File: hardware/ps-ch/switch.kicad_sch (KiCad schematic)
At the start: 18 parts, among them Q4 PSMN059-150Y, Q9 PSMN059-150Y, U16 LM74502H, U18 74LVC126A, U20 74LVC126A

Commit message: improved circuit
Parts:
- U20: footprint (none) -> Package_SO:TSSOP-14_4.4x5mm_P0.65mm; Manufacturer (none) -> Nexperia; Manufacturer Part Number (none) -> 74LVC126APW,118
- U20: renamed from U18; footprint (none) -> Package_SO:TSSOP-14_4.4x5mm_P0.65mm; Manufacturer (none) -> Nexperia; Manufacturer Part Number (none) -> 74LVC126APW,118
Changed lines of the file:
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@@
 			)
 		)
-		(property "Footprint" ""
+		(property "Footprint" "Package_SO:TSSOP-14_4.4x5mm_P0.65mm"
 			(at 147.32 167.64 0)
 			(effects
@@
 			)
 		)
-		(property "Datasheet" ""
+		(property "Datasheet" "https://assets.nexperia.com/documents/data-sheet/74LVC126A.pdf"
 			(at 147.32 167.64 0)
 			(effects
@@
 		)
 		(property "Description" ""
+			(at 147.32 167.64 0)
+			(effects
+				(font
+					(size 1.27 1.27)
+				)
+				(hide yes)
+			)
+		)
+		(property "Manufacturer" "Nexperia"
+			(at 147.32 167.64 0)
+			(effects
+				(font
+					(size 1.27 1.27)
+				)
+				(hide yes)
+			)
+		)
+		(property "Manufacturer Part Number" "74LVC126APW,118"
 			(at 147.32 167.64 0)
 			(effects
@@
 			)
 		)
-		(property "Footprint" ""
+		(property "Footprint" "Package_SO:TSSOP-14_4.4x5mm_P0.65mm"
 			(at 63.5 167.64 0)
 			(effects
@@
 			)
 		)
-		(property "Datasheet" ""
+		(property "Datasheet" "https://assets.nexperia.com/documents/data-sheet/74LVC126A.pdf"
 			(at 63.5 167.64 0)
 			(effects
@@
 		)
 		(property "Description" ""
+			(at 63.5 167.64 0)
+			(effects
+				(font
+					(size 1.27 1.27)
+				)
+				(hide yes)
+			)
+		)
+		(property "Manufacturer" "Nexperia"
+			(at 63.5 167.64 0)
+			(effects
+				(font
+					(size 1.27 1.27)
+				)
+				(hide yes)
+			)
+		)
+		(property "Manufacturer Part Number" "74LVC126APW,118"
 			(at 63.5 167.64 0)
 			(effects
@@
 			)
 		)
-		(property "Footprint" ""
+		(property "Footprint" "Package_SO:TSSOP-14_4.4x5mm_P0.65mm"
 			(at 96.52 167.64 0)
 			(effects
@@
 			)
 		)
-		(property "Datasheet" ""
+		(property "Datasheet" "https://assets.nexperia.com/documents/data-sheet/74LVC126A.pdf"
 			(at 96.52 167.64 0)
 			(effects
@@
 		)
 		(property "Description" ""
+			(at 96.52 167.64 0)
+			(effects
+				(font
+					(size 1.27 1.27)
+				)
+				(hide yes)
+			)
+		)
+		(property "Manufacturer" "Nexperia"
+			(at 96.52 167.64 0)
+			(effects
+				(font
+					(size 1.27 1.27)
+				)
+				(hide yes)
+			)
+		)
+		(property "Manufacturer Part Number" "74LVC126APW,118"
 			(at 96.52 167.64 0)
 			(effects
@@
 		(dnp no)
 		(fields_autoplaced yes)
-		(property "Reference" "U18"
+		(property "Reference" "U20"
 			(at 143.51 107.8798 0)
 			(effects
@@
 			)
 		)
-		(property "Footprint" ""
+		(property "Footprint" "Package_SO:TSSOP-14_4.4x5mm_P0.65mm"
 			(at 132.08 114.3 0)
 			(effects
@@
 			)
 		)
-		(property "Datasheet" ""
+		(property "Datasheet" "https://assets.nexperia.com/documents/data-sheet/74LVC126A.pdf"
 			(at 132.08 114.3 0)
 			(effects
@@
 			)
 		)
+		(property "Manufacturer" "Nexperia"
+			(at 132.08 114.3 0)
+			(effects
+				(font
+					(size 1.27 1.27)
+				)
+				(hide yes)
+			)
+		)
+		(property "Manufacturer Part Number" "74LVC126APW,118"
+			(at 132.08 114.3 0)
+			(effects
+				(font
+					(size 1.27 1.27)
+				)
+				(hide yes)
+			)
+		)
 		(pin "5"
 		)
@@
 			(project "ps-ch"
 				(path "/431acd2e-2ab9-4aa9-b759-273f044decc5/8b075681-8e5e-4240-bfaa-b14997f80de9"
-					(reference "U18")
+					(reference "U20")
 					(unit 1)
 				)

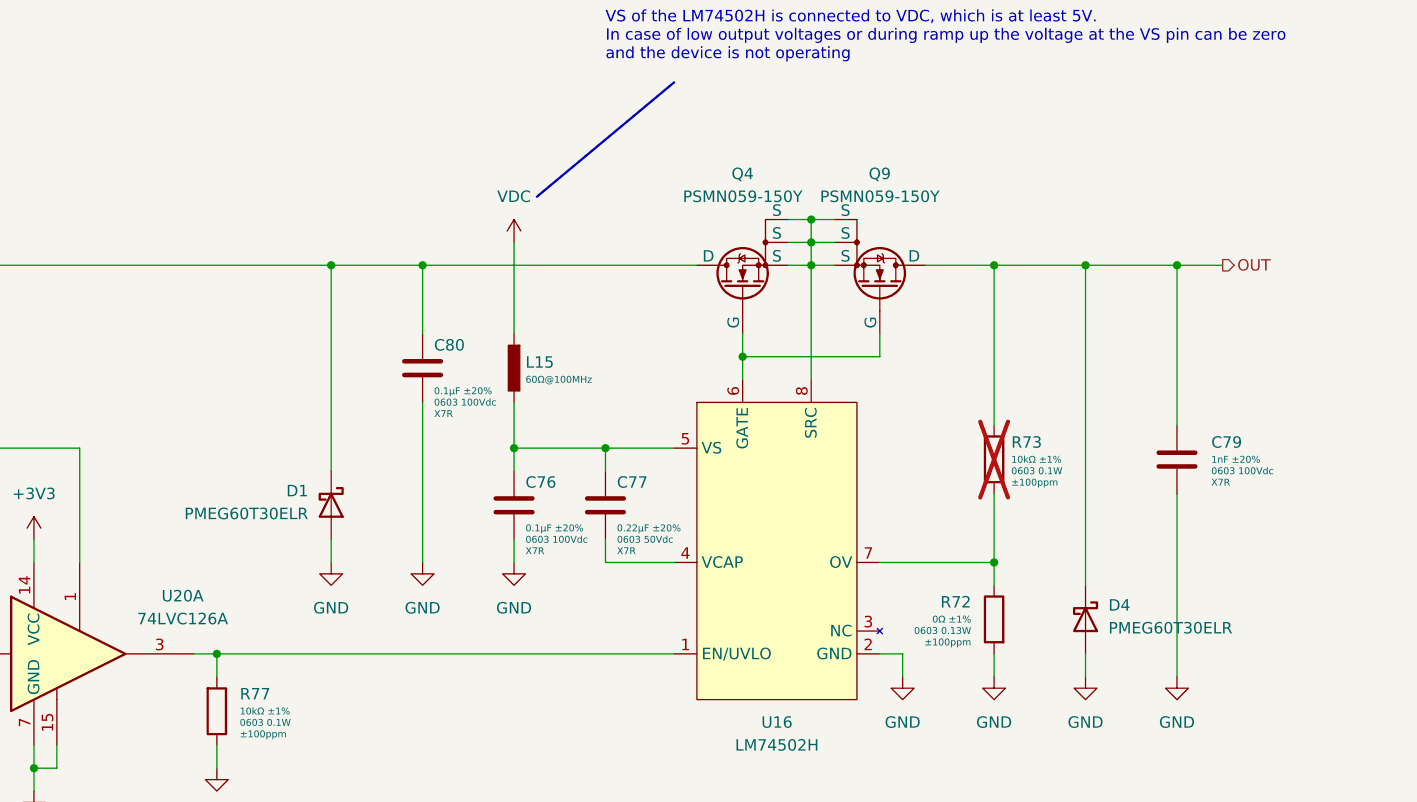
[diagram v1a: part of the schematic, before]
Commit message: added snubber circuit components
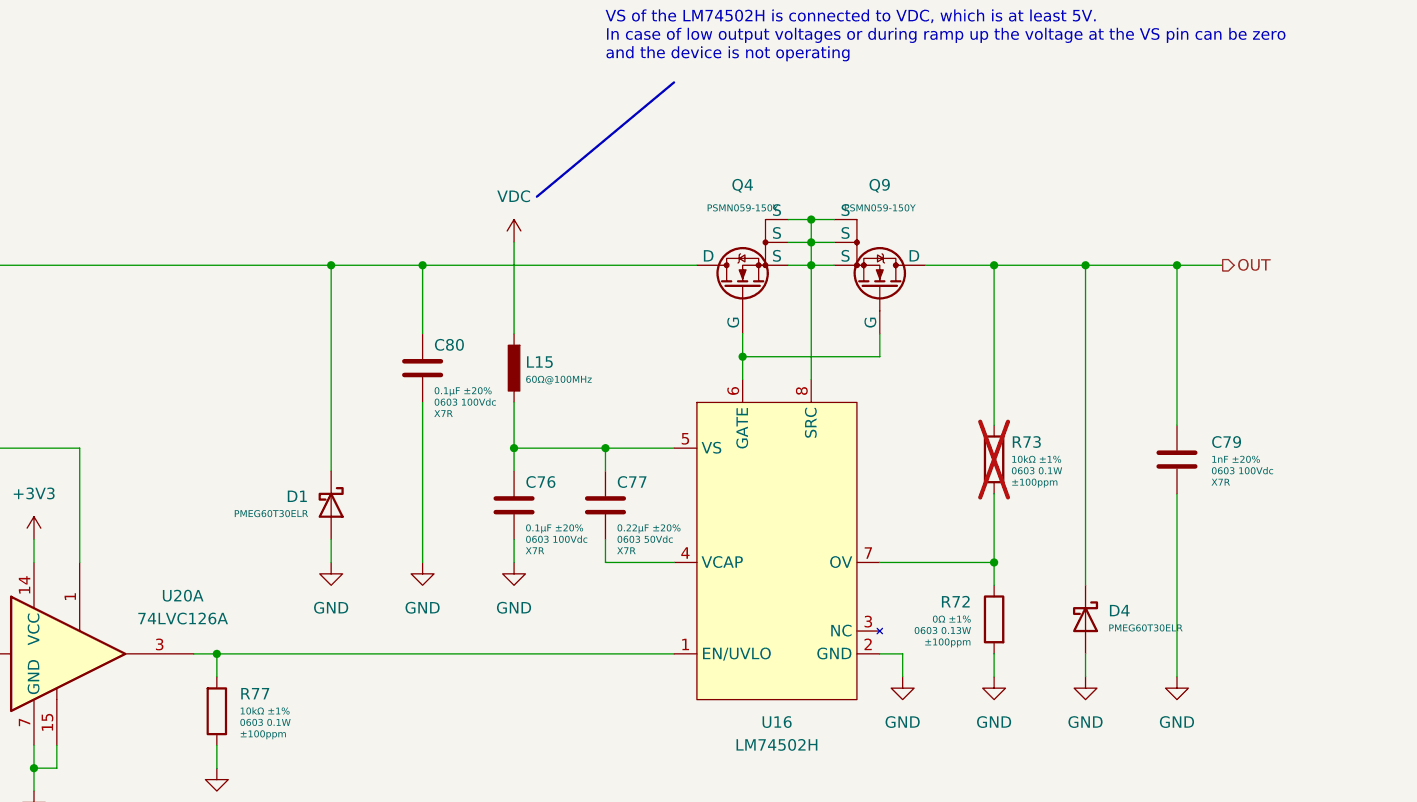
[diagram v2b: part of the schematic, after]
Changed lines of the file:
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@@
 		(on_board yes)
 		(dnp no)
+		(fields_autoplaced yes)
 		(property "Reference" "Q9"
-			(at 220.98 60.96 90)
+			(at 220.98 62.23 90)
 			(effects
 				(font
@@
 		)
 		(property "Value" "PSMN059-150Y"
-			(at 220.98 63.5 90)
-			(effects
-				(font
-					(size 1.27 1.27)
+			(at 220.98 64.77 90)
+			(effects
+				(font
+					(size 0.762 0.762)
+					(color 132 0 132 1)
 				)
 			)
@@
 		(fields_autoplaced yes)
 		(property "Reference" "Q4"
-			(at 205.74 60.96 90)
+			(at 205.74 62.23 90)
 			(effects
 				(font
@@
 		)
 		(property "Value" "PSMN059-150Y"
-			(at 205.74 63.5 90)
-			(effects
-				(font
-					(size 1.27 1.27)
+			(at 205.74 64.77 90)
+			(effects
+				(font
+					(size 0.762 0.762)
+					(color 132 0 132 1)
 				)
 			)
@@
 		(fields_autoplaced yes)
 		(property "Reference" "D1"
-			(at 157.48 96.2024 90)
+			(at 157.48 96.8374 90)
 			(effects
 				(font
@@
 		)
 		(property "Value" "PMEG60T30ELR"
-			(at 157.48 98.7424 90)
-			(effects
-				(font
-					(size 1.27 1.27)
+			(at 157.48 98.7425 90)
+			(effects
+				(font
+					(size 0.762 0.762)
+					(color 132 0 132 1)
 				)
 				(justify right)
@@
 		(fields_autoplaced yes)
 		(property "Reference" "D4"
-			(at 246.38 108.9024 90)
+			(at 246.38 109.5374 90)
 			(effects
 				(font
@@
 		)
 		(property "Value" "PMEG60T30ELR"
-			(at 246.38 111.4424 90)
-			(effects
-				(font
-					(size 1.27 1.27)
-				)
-				(justify left)
+			(at 246.38 111.4425 90)
+			(effects
+				(font
+					(size 0.762 0.762)
+					(color 132 0 132 1)
+				)
+				(justify left)

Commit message: created and assigned footprints
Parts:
- Q4, Q9: footprint (none) -> ps-ch:SOT669; Manufacturer (none) -> Nexperia; Manufacturer Part Number (none) -> PSMN059-150Y,115
- U16: footprint (none) -> Package_TO_SOT_SMD:SOT-23-8; Manufacturer (none) -> Texas Instruments; Manufacturer Part Number (none) -> LM74502HDDFR
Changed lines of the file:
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@@
 			)
 		)
-		(property "Footprint" ""
+		(property "Footprint" "Package_TO_SOT_SMD:SOT-23-8"
 			(at 200.66 86.36 0)
 			(effects
@@
 		)
 		(property "Description" ""
+			(at 200.66 86.36 0)
+			(effects
+				(font
+					(size 1.27 1.27)
+				)
+				(hide yes)
+			)
+		)
+		(property "Manufacturer" "Texas Instruments"
+			(at 200.66 86.36 0)
+			(effects
+				(font
+					(size 1.27 1.27)
+				)
+				(hide yes)
+			)
+		)
+		(property "Manufacturer Part Number" "LM74502HDDFR"
 			(at 200.66 86.36 0)
 			(effects
@@
 			)
 		)
-		(property "Footprint" ""
+		(property "Footprint" "ps-ch:SOT669"
 			(at 223.52 68.58 0)
 			(effects
@@
 			)
 		)
-		(property "Datasheet" "https://ngspice.sourceforge.io/docs/ngspice-html-manual/manual.xhtml#cha_MOSFETs"
+		(property "Datasheet" "https://assets.nexperia.com/documents/data-sheet/PSMN059-150Y.pdf"
 			(at 208.28 73.66 0)
 			(effects
@@
 		(property "Sim.Pins" "1=D 2=G 3=S"
 			(at 205.74 73.66 0)
+			(effects
+				(font
+					(size 1.27 1.27)
+				)
+				(hide yes)
+			)
+		)
+		(property "Manufacturer" "Nexperia"
+			(at 220.98 73.66 0)
+			(effects
+				(font
+					(size 1.27 1.27)
+				)
+				(hide yes)
+			)
+		)
+		(property "Manufacturer Part Number" "PSMN059-150Y,115"
+			(at 220.98 73.66 0)
 			(effects
 				(font
@@
 			)
 		)
-		(property "Footprint" ""
+		(property "Footprint" "ps-ch:SOT669"
 			(at 203.2 68.58 0)
 			(effects
@@
 			)
 		)
-		(property "Datasheet" "https://ngspice.sourceforge.io/docs/ngspice-html-manual/manual.xhtml#cha_MOSFETs"
+		(property "Datasheet" "https://assets.nexperia.com/documents/data-sheet/PSMN059-150Y.pdf"
 			(at 218.44 73.66 0)
 			(effects
@@
 			(effects
 				(font
+					(size 1.27 1.27)
+				)
+				(hide yes)
+			)
+		)
+		(property "Manufacturer" "Nexperia"
+			(at 205.74 73.66 0)
+			(effects
+				(font
+					(size 1.27 1.27)
+				)
+				(hide yes)
+			)
+		)
+		(property "Manufacturer Part Number" "PSMN059-150Y,115"
+			(at 205.74 73.66 0)
+			(effects
+				(font

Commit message: first pcb sync
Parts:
- renumbered C80 to C72, C79 to C73, C76 to C74, C77 to C75, D1 to D6, D4 to D7, L15 to L12, Q4 to Q7, Q9 to Q8, R73 to R55, R72 to R56, R76 to R57, R77 to R58, R28 to R59, R78 to R60, U16 to U13, U20 to U14
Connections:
- net GND: no longer U14.15

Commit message: started floorplanning
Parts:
- added C81: 0.1μF 0603 100Vdc X7R ±20%, Capacitor_SMD:C_0603_1608Metric, symbol ps-ch:0.1μF 0603 100Vdc X7R ±20%
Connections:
- net +3V3: now also C81.2
- net GND: now also C81.1
